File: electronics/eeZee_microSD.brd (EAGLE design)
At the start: 27.8 x 18.3 mm, 12 parts, among them U1 MIC5317, U2 74HC4050, U4 MICROSD_CD

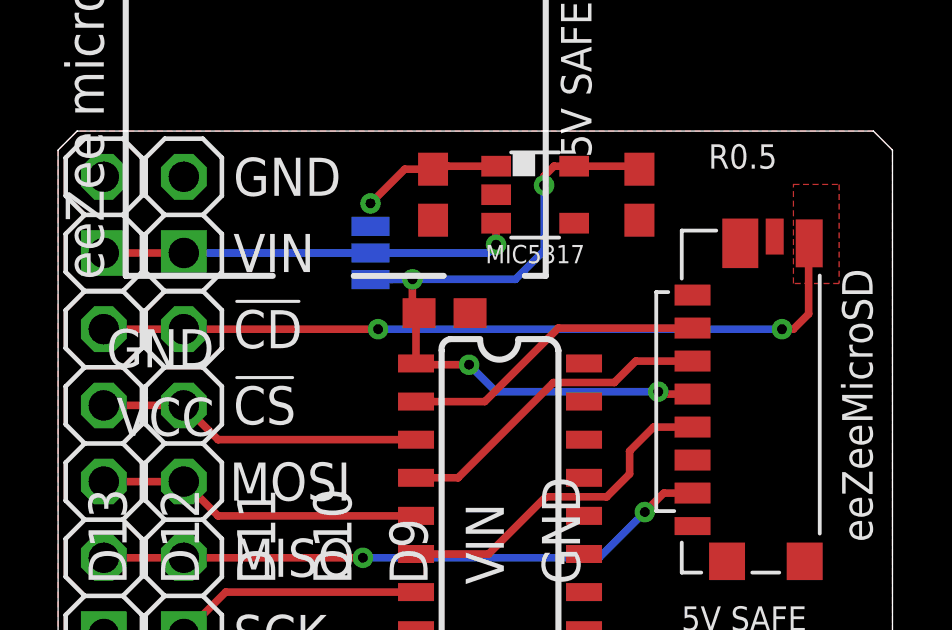
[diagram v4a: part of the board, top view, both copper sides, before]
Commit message: revised byp/reg label, created gerbers, zip
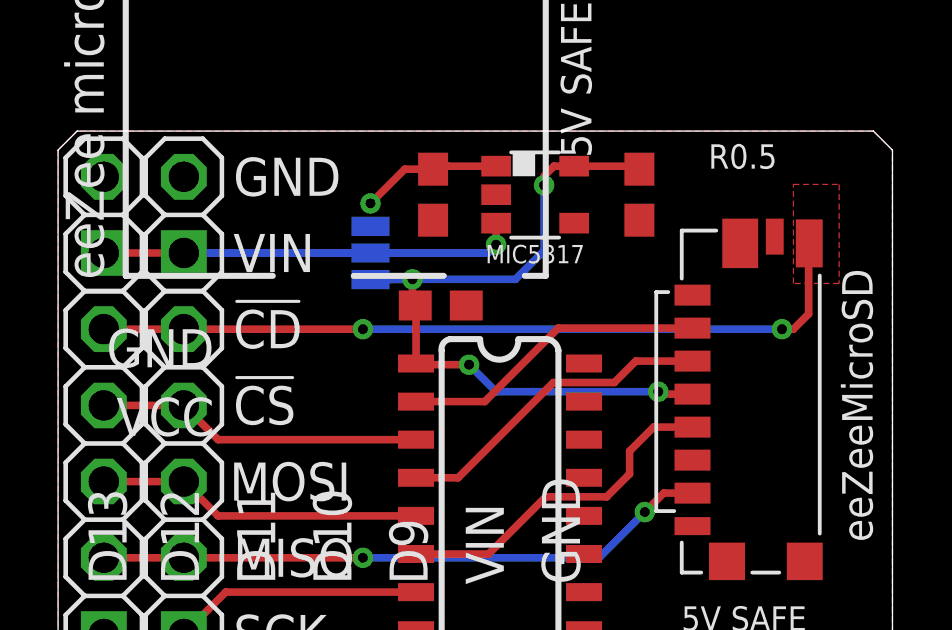
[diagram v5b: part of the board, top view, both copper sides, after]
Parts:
- moved C3 0.28 mm to (12.8, 12.5)
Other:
- board text added: "SD"
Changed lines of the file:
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@@
 <text x="5.588" y="1.524" size="1.27" layer="26" font="vector" rot="MR0" align="center-right">SCK</text>
 <text x="5.588" y="11.684" size="1.27" layer="26" font="vector" rot="MR0" align="center-right">!CD</text>
-<text x="11.39" y="11.701" size="0.8128" layer="26" font="vector" ratio="10" rot="MR0">BYP</text>
+<text x="11.009" y="11.574" size="0.8128" layer="26" font="vector" ratio="10" rot="MR0">SD</text>
 <text x="11.39" y="16.019" size="0.8128" layer="26" font="vector" ratio="10" rot="MR0">REG</text>
 </plain>
@@
 <attribute name="VALUE" x="14.351" y="8.509" size="0.8128" layer="27" font="vector" ratio="10" rot="R270"/>
 </element>
-<element name="C3" library="rcl" package="C0603" value="104" x="12.8828" y="12.219" smashed="yes">
-<attribute name="PARTNO" value="LMK107B7105KA-T" x="12.8828" y="12.219" size="1.778" layer="27" display="off"/>
-<attribute name="DATABASE" value="./../../../eagle/PARTSDB.TXT" x="12.8828" y="12.219" size="1.778" layer="27" display="off"/>
-<attribute name="VALUE" x="12.9" y="13" size="0.6096" layer="27" font="vector" ratio="10" align="bottom-center"/>
+<element name="C3" library="rcl" package="C0603" value="104" x="12.7558" y="12.473" smashed="yes">
+<attribute name="PARTNO" value="LMK107B7105KA-T" x="12.7558" y="12.473" size="1.778" layer="27" display="off"/>
+<attribute name="DATABASE" value="./../../../eagle/PARTSDB.TXT" x="12.7558" y="12.473" size="1.778" layer="27" display="off"/>
+<attribute name="VALUE" x="12.773" y="13.254" size="0.6096" layer="27" font="vector" ratio="10" align="bottom-center"/>
 </element>
 <element name="JP2" library="pinhead-2" package="1X02-S" value="PWR" x="1.524" y="15.494" smashed="yes" rot="R90"/>
@@
 <wire x1="11.973" y1="10.5" x2="11.932" y2="10.541" width="0.254" layer="1"/>
 <wire x1="11.932" y1="10.541" x2="11.932" y2="12.1182" width="0.254" layer="1"/>
-<wire x1="11.932" y1="12.1182" x2="12.0328" y2="12.219" width="0.254" layer="1"/>
+<wire x1="11.932" y1="12.1182" x2="11.9058" y2="12.473" width="0.254" layer="1"/>
 <wire x1="11.814" y1="13.346" x2="11.8058" y2="12.446" width="0.254" layer="1"/>
-<wire x1="11.8058" y1="12.446" x2="12.0328" y2="12.219" width="0.254" layer="1"/>
+<wire x1="11.8058" y1="12.446" x2="11.9058" y2="12.473" width="0.254" layer="1"/>
 <contactref element="U1" pad="5"/>
 <contactref element="C1" pad="1"/>
@@
 <wire x1="25.019" y1="12.192" x2="25.019" y2="14.826" width="0.254" layer="1"/>
 <wire x1="25.019" y1="14.826" x2="25.039" y2="14.546" width="0.254" layer="1"/>
-<wire x1="4.191" y1="11.684" x2="10.668" y2="11.684" width="0.254" layer="1"/>
-<via x="10.668" y="11.684" extent="1-16" drill="0.3302"/>
-<wire x1="10.668" y1="11.684" x2="24.13" y2="11.684" width="0.254" layer="16"/>
+<wire x1="4.191" y1="11.684" x2="10.16" y2="11.684" width="0.254" layer="1"/>
+<via x="10.16" y="11.684" extent="1-16" drill="0.3302"/>
+<wire x1="10.16" y1="11.684" x2="24.13" y2="11.684" width="0.254" layer="16"/>
 <via x="24.13" y="11.684" extent="1-16" drill="0.3302"/>
 <wire x1="24.13" y1="11.684" x2="24.511" y2="11.684" width="0.254" layer="1"/>
